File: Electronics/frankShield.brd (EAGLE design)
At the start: 68.6 x 53.3 mm, 24 parts, among them IC1 BD6230F, IC2 BD6230F, IC3 TS5A23157

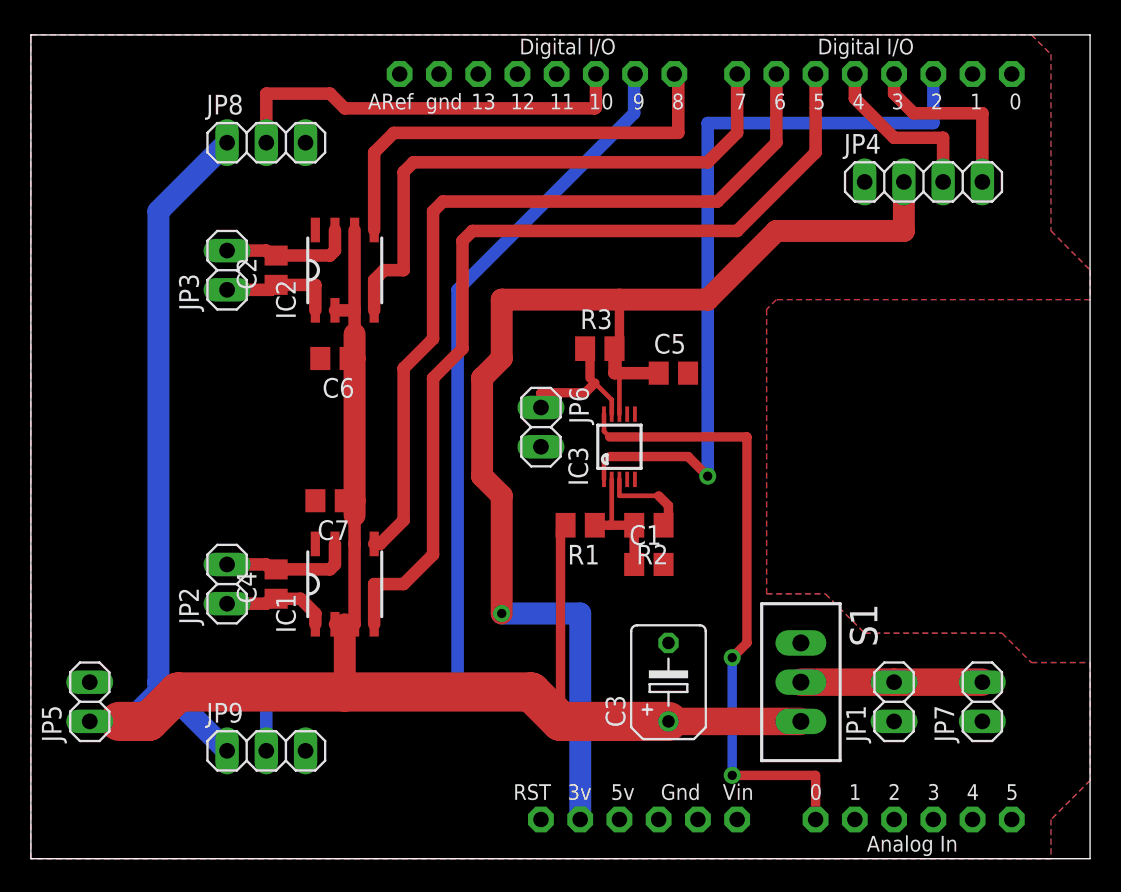
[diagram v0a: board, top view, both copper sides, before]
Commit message: Added LED to shield, and anti-short safety diode to the charge circuit.
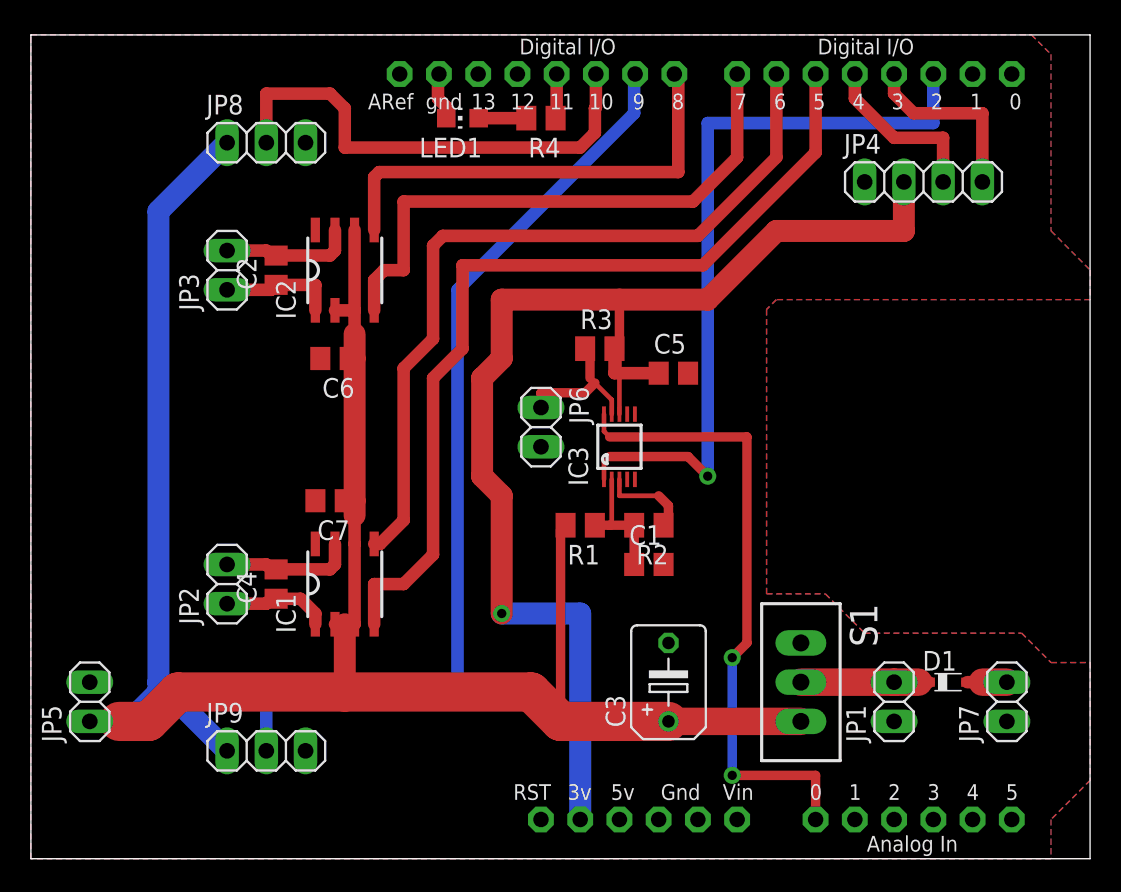
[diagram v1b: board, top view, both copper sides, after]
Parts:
- added D1: BAT60J, diode:SOD323_ST
- added LED1: (no value), led:CHIP-LED0805
- added R4: 180R, rcl:M0805
- moved JP7 1.59 mm to (63.2, 10.2)
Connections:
- new net N$16: D1.A, JP7.2
- new net N$19: LED1.A, R4.2
- new net N$20: R4.1, U$1.D11
- net GND: now also LED1.C
- net N$13: now also D1.C; no longer JP7.2
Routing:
- net N$18: track 27.1 -> 31.6 mm
- net N$13: track 11.7 -> 8.28 mm
- net GND: track 5.90 -> 9.01 mm
- net N$19: track 0.00 -> 3.08 mm
- net N$20: track 0.00 -> 2.88 mm
- net N$16: track 0.00 -> 2.56 mm
- net N$8: track 58.6 -> 57.7 mm
- net N$7: track 51.8 -> 51.1 mm
- net N$10: track 29.1 -> 29.7 mm
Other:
- board text added: "+batt"
- board text added: "EPS8266/Arduino Shield V1.1 reprapltd.com Mechanics & software: Sally Bowyer Electronics: Adrian Bowyer Licence - GPL"
- board text removed: "EPS8266/Arduino Shield V1.0 reprapltd.com Mechanics & software: Sally Bowyer Electronics: Adrian Bowyer Licence - GPL"
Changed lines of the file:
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@@
 <layer number="23" name="tOrigins" color="15" fill="1" visible="yes" active="yes"/>
 <layer number="24" name="bOrigins" color="15" fill="1" visible="yes" active="yes"/>
-<layer number="25" name="tNames" color="7" fill="1" visible="no" active="yes"/>
+<layer number="25" name="tNames" color="7" fill="1" visible="yes" active="yes"/>
 <layer number="26" name="bNames" color="7" fill="1" visible="yes" active="yes"/>
 <layer number="27" name="tValues" color="7" fill="1" visible="yes" active="yes"/>
@@
 <text x="60.6425" y="16.8275" size="1.27" layer="27" rot="R90">Frank The Robot
 </text>
-<text x="7.9375" y="19.685" size="1.016" layer="27" rot="R90">EPS8266/Arduino Shield V1.0
+<text x="7.9375" y="19.685" size="1.016" layer="27" rot="R90">EPS8266/Arduino Shield V1.1
 reprapltd.com
 Mechanics &amp; software: Sally Bowyer
@@
 <text x="15.5575" y="42.545" size="1.016" layer="27" rot="R90">sig</text>
 <text x="15.5575" y="8.89" size="1.016" layer="27" rot="R90">sig</text>
-<text x="13.335" y="40.9575" size="1.016" layer="27" rot="R90">+3V3</text>
-<text x="13.335" y="8.89" size="1.016" layer="27" rot="R90">+3V3</text>
+<text x="13.0175" y="41.275" size="1.016" layer="27" rot="R90">+batt</text>
+<text x="13.0175" y="8.89" size="1.016" layer="27" rot="R90">+batt</text>
 </plain>
 <attributes>
@@
 <element name="C1" library="rcl" package="C0805" value="1uF" x="40.005" y="19.05"/>
 <element name="S1" library="switch" package="TL3XPO" value="TL36PO" x="49.8475" y="11.43" rot="R270"/>
-<element name="JP7" library="pinhead" package="1X02" value="" x="61.595" y="10.16" rot="R90"/>
+<element name="JP7" library="pinhead" package="1X02" value="" x="63.1825" y="10.16" rot="R90"/>
 <element name="JP8" library="pinhead" package="1X03" value="" x="15.24" y="46.355"/>
 <element name="JP9" library="pinhead" package="1X03" value="" x="15.24" y="6.985"/>
@@
 </element>
 <element name="C7" library="rcl" package="C0805" value="0.1uF" x="19.3675" y="23.1775" rot="R180"/>
+<element name="D1" library="diode" package="SOD323_ST" value="BAT60J" x="59.3725" y="11.43"/>
+<element name="LED1" library="led" package="CHIP-LED0805" value="" x="27.94" y="47.9425" rot="R90"/>
+<element name="R4" library="rcl" package="M0805" value="180R" x="33.02" y="47.9425" rot="R180"/>
 </elements>
 <signals>
@@
 <vertex x="51.435" y="17.145"/>
 <vertex x="53.975" y="14.605"/>
-<vertex x="62.865" y="14.605"/>
-<vertex x="64.77" y="12.7"/>
+<vertex x="64.135" y="14.605"/>
+<vertex x="66.04" y="12.7"/>
 <vertex x="68.58" y="12.7"/>
 <vertex x="68.58" y="5.08"/>
@@
 <vertex x="51.435" y="17.145"/>
 <vertex x="53.975" y="14.605"/>
-<vertex x="62.865" y="14.605"/>
-<vertex x="64.77" y="12.7"/>
+<vertex x="64.135" y="14.605"/>
+<vertex x="66.04" y="12.7"/>
 <vertex x="68.58" y="12.7"/>
 <vertex x="68.58" y="5.08"/>
@@
 <contactref element="C6" pad="2"/>
 <contactref element="C7" pad="2"/>
+<contactref element="LED1" pad="C"/>
+<wire x1="26.89" y1="47.9425" x2="26.89" y2="48.675" width="0.8128" layer="1"/>
+<wire x1="26.89" y1="48.675" x2="26.3525" y2="49.2125" width="0.8128" layer="1"/>
+<wire x1="26.3525" y1="49.2125" x2="26.3525" y2="50.7365" width="0.8128" layer="1"/>
+<wire x1="26.3525" y1="50.7365" x2="26.416" y2="50.8" width="0.8128" layer="1"/>
 </signal>
 <signal name="VIN">
@@
 <contactref element="IC1" pad="5"/>
 <contactref element="U$1" pad="D6"/>
-<wire x1="48.26" y1="50.8" x2="48.26" y2="46.355" width="0.8128" layer="1"/>
-<wire x1="48.26" y1="46.355" x2="44.45" y2="42.545" width="0.8128" layer="1"/>
-<wire x1="44.45" y1="42.545" x2="26.67" y2="42.545" width="0.8128" layer="1"/>
-<wire x1="26.67" y1="42.545" x2="26.035" y2="41.91" width="0.8128" layer="1"/>
-<wire x1="26.035" y1="41.91" x2="26.035" y2="33.655" width="0.8128" layer="1"/>
+<wire x1="48.26" y1="50.8" x2="48.26" y2="45.4025" width="0.8128" layer="1"/>
+<wire x1="48.26" y1="45.4025" x2="43.18" y2="40.3225" width="0.8128" layer="1"/>
 <wire x1="26.035" y1="33.655" x2="24.13" y2="31.75" width="0.8128" layer="1"/>
 <wire x1="24.13" y1="31.75" x2="24.13" y2="21.9075" width="0.8128" layer="1"/>
 <wire x1="22.225" y1="20.38" x2="22.6025" y2="20.38" width="0.8128" layer="1"/>
 <wire x1="22.6025" y1="20.38" x2="24.13" y2="21.9075" width="0.8128" layer="1"/>
+<wire x1="43.18" y1="40.3225" x2="26.67" y2="40.3225" width="0.8128" layer="1"/>
+<wire x1="26.67" y1="40.3225" x2="26.035" y2="39.6875" width="0.8128" layer="1"/>
+<wire x1="26.035" y1="39.6875" x2="26.035" y2="33.655" width="0.8128" layer="1"/>
 </signal>
 <signal name="N$8">
@@
 <contactref element="U$1" pad="D5"/>
 <wire x1="50.8" y1="50.8" x2="50.8" y2="45.72" width="0.8128" layer="1"/>
-<wire x1="50.8" y1="45.72" x2="45.72" y2="40.64" width="0.8128" layer="1"/>
-<wire x1="45.72" y1="40.64" x2="28.575" y2="40.64" width="0.8128" layer="1"/>
-<wire x1="28.575" y1="40.64" x2="27.94" y2="40.005" width="0.8128" layer="1"/>
-<wire x1="27.94" y1="40.005" x2="27.94" y2="33.02" width="0.8128" layer="1"/>
+<wire x1="50.8" y1="45.72" x2="43.4975" y2="38.4175" width="0.8128" layer="1"/>
+<wire x1="27.94" y1="38.4175" x2="27.94" y2="33.02" width="0.8128" layer="1"/>
 <wire x1="27.94" y1="33.02" x2="26.035" y2="31.115" width="0.8128" layer="1"/>
 <wire x1="26.035" y1="31.115" x2="26.035" y2="19.685" width="0.8128" layer="1"/>
@@
 <wire x1="24.13" y1="17.78" x2="22.225" y2="17.78" width="0.8128" layer="1"/>
 <wire x1="22.225" y1="17.78" x2="22.225" y2="15.18" width="0.8128" layer="1"/>
+<wire x1="43.4975" y1="38.4175" x2="27.94" y2="38.4175" width="0.8128" layer="1"/>
 </signal>
 <signal name="N$9">
 <contactref element="U$1" pad="D7"/>
 <contactref element="IC2" pad="4"/>
-<wire x1="45.72" y1="50.8" x2="45.72" y2="46.99" width="0.8128" layer="1"/>
-<wire x1="45.72" y1="46.99" x2="43.815" y2="45.085" width="0.8128" layer="1"/>
-<wire x1="43.815" y1="45.085" x2="24.765" y2="45.085" width="0.8128" layer="1"/>
-<wire x1="24.765" y1="45.085" x2="24.13" y2="44.45" width="0.8128" layer="1"/>
-<wire x1="24.13" y1="44.45" x2="24.13" y2="38.1" width="0.8128" layer="1"/>
+<wire x1="45.72" y1="50.8" x2="45.72" y2="45.4025" width="0.8128" layer="1"/>
+<wire x1="45.72" y1="45.4025" x2="42.8625" y2="42.545" width="0.8128" layer="1"/>
+<wire x1="24.13" y1="42.545" x2="24.13" y2="38.1" width="0.8128" layer="1"/>
 <wire x1="24.13" y1="38.1" x2="22.86" y2="38.1" width="0.8128" layer="1"/>
 <wire x1="22.86" y1="38.1" x2="22.225" y2="37.465" width="0.8128" layer="1"/>
 <wire x1="22.225" y1="37.465" x2="22.225" y2="35.5" width="0.8128" layer="1"/>
+<wire x1="42.8625" y1="42.545" x2="24.13" y2="42.545" width="0.8128" layer="1"/>
 </signal>
 <signal name="N$10">
 <contactref element="U$1" pad="D8"/>
 <contactref element="IC2" pad="5"/>
-<wire x1="22.225" y1="40.7" x2="22.225" y2="45.72" width="0.8128" layer="1"/>
-<wire x1="22.225" y1="45.72" x2="23.495" y2="46.99" width="0.8128" layer="1"/>
-<wire x1="23.495" y1="46.99" x2="41.91" y2="46.99" width="0.8128" layer="1"/>
-<wire x1="41.91" y1="46.99" x2="41.91" y2="50.546" width="0.8128" layer="1"/>
+<wire x1="22.225" y1="40.7" x2="22.225" y2="44.1325" width="0.8128" layer="1"/>
+<wire x1="41.91" y1="44.45" x2="41.91" y2="50.546" width="0.8128" layer="1"/>
 <wire x1="41.91" y1="50.546" x2="41.656" y2="50.8" width="0.8128" layer="1"/>
+<wire x1="41.91" y1="44.45" x2="22.5425" y2="44.45" width="0.8128" layer="1"/>
+<wire x1="22.5425" y1="44.45" x2="22.225" y2="44.1325" width="0.8128" layer="1"/>
 </signal>
 <signal name="5V">
@@
 <contactref element="JP1" pad="2"/>
 <wire x1="49.8475" y1="11.43" x2="55.88" y2="11.43" width="1.778" layer="1"/>
-<contactref element="JP7" pad="2"/>
-<wire x1="55.88" y1="11.43" x2="61.595" y2="11.43" width="1.778" layer="1"/>
+<contactref element="D1" pad="C"/>
+<wire x1="58.1225" y1="11.43" x2="57.4675" y2="11.43" width="0.8128" layer="1"/>
+<wire x1="57.4675" y1="11.43" x2="55.88" y2="11.43" width="1.778" layer="1"/>
 </signal>
 <signal name="N$17">
@@
 <wire x1="36.576" y1="50.8" x2="36.576" y2="48.641" width="0.8128" layer="1"/>
 <wire x1="36.576" y1="48.641" x2="36.5125" y2="48.5775" width="0.8128" layer="1"/>
-<wire x1="36.5125" y1="48.5775" x2="20.32" y2="48.5775" width="0.8128" layer="1"/>
 <wire x1="20.32" y1="48.5775" x2="19.3675" y2="49.53" width="0.8128" layer="1"/>
 <wire x1="19.3675" y1="49.53" x2="15.24" y2="49.53" width="0.8128" layer="1"/>
 <wire x1="15.24" y1="49.53" x2="15.24" y2="46.355" width="0.8128" layer="1"/>
+<wire x1="36.5125" y1="48.5775" x2="36.5125" y2="46.99" width="0.8128" layer="1"/>
+<wire x1="36.5125" y1="46.99" x2="35.56" y2="46.0375" width="0.8128" layer="1"/>
+<wire x1="35.56" y1="46.0375" x2="20.32" y2="46.0375" width="0.8128" layer="1"/>
+<wire x1="20.32" y1="46.0375" x2="20.32" y2="48.5775" width="0.8128" layer="1"/>
 </signal>
 <signal name="N$3">
@@
 <wire x1="15.24" y1="19.05" x2="12.7" y2="19.05" width="0.8128" layer="1"/>
 </signal>
+<signal name="N$16">
+<contactref element="JP7" pad="2"/>
+<contactref element="D1" pad="A"/>
+<wire x1="63.1825" y1="11.43" x2="61.595" y2="11.43" width="1.778" layer="1"/>
+<wire x1="61.595" y1="11.43" x2="60.6225" y2="11.43" width="0.8128" layer="1"/>
+</signal>
+<signal name="N$19">
+<contactref element="R4" pad="2"/>
+<contactref element="LED1" pad="A"/>
+<wire x1="32.07" y1="47.9425" x2="28.99" y2="47.9425" width="0.8128" layer="1"/>
+</signal>
+<signal name="N$20">
+<contactref element="R4" pad="1"/>
+<contactref element="U$1" pad="D11"/>
+<wire x1="34.036" y1="50.8" x2="34.036" y2="48.0085" width="0.8128" layer="1"/>
+<wire x1="34.036" y1="48.0085" x2="33.97" y2="47.9425" width="0.8128" layer="1"/>
+</signal>
 </signals>
